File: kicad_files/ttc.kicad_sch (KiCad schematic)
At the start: 17 parts, among them J8 5051101592, J9 Conn_01x02, Q8 Q_NMOS_DGS, SW1 SW_DPST, U10 RFM98PW, U9 505110-0697

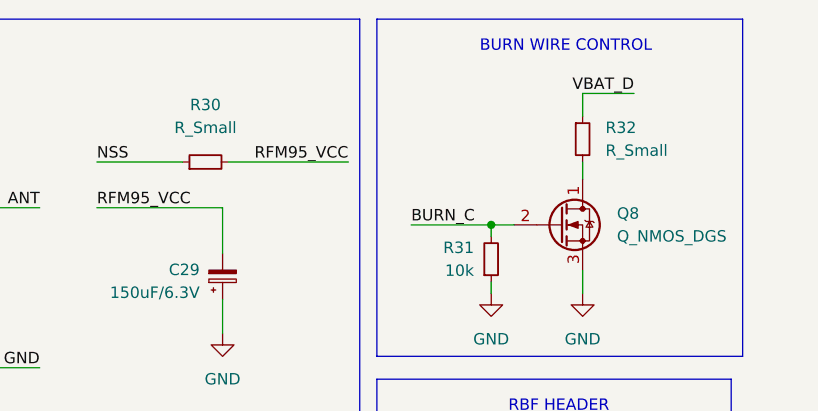
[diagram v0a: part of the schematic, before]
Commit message: update components values
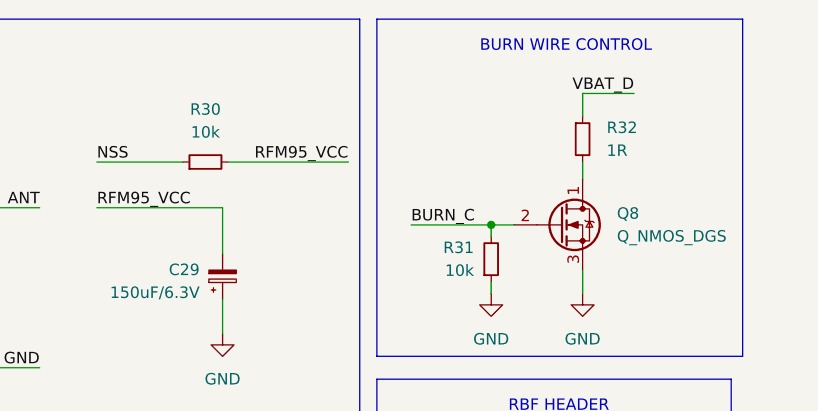
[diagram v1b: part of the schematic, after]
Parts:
- R30: value R_Small -> 10k
- R32: value R_Small -> 1R
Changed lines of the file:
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@@
   (symbol (lib_id "Device:R_Small") (at 196.723 56.642 90) (unit 1)
     (in_bom yes) (on_board yes) (fields_autoplaced)
-    (property "Reference" "R30" (id 0) (at 196.723 50.292 90))
-    (property "Value" "R_Small" (id 1) (at 196.723 52.832 90))
+    (property "Reference" "R30" (id 0) (at 196.723 50.8 90))
+    (property "Value" "10k" (id 1) (at 196.723 53.34 90))
     (property "Footprint" "Resistor_SMD:R_0402_1005Metric" (id 2) (at 196.723 56.642 0)
       (effects (font (size 1.27 1.27)) hide)
@@
   )
   (symbol (lib_id "Device:R_Small") (at 238.633 54.102 0) (unit 1)
-    (in_bom yes) (on_board yes) (fields_autoplaced)
-    (property "Reference" "R32" (id 0) (at 241.173 52.8319 0)
+    (in_bom yes) (on_board yes)
+    (property "Reference" "R32" (id 0) (at 241.3 52.8319 0)
       (effects (font (size 1.27 1.27)) (justify left))
     )
-    (property "Value" "R_Small" (id 1) (at 241.173 55.3719 0)
+    (property "Value" "1R" (id 1) (at 241.3 55.3719 0)
       (effects (font (size 1.27 1.27)) (justify left))
     )
